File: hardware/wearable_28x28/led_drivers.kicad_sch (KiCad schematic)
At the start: 22 parts, among them U101 MBI5124GP-B, U102 MBI5124GP-B, U103 MBI5124GP-B, U104 MBI5124GP-B, U105 MBI5124GP-B, U106 MBI5124GP-B, U107 SN74LVC1G125DBVR

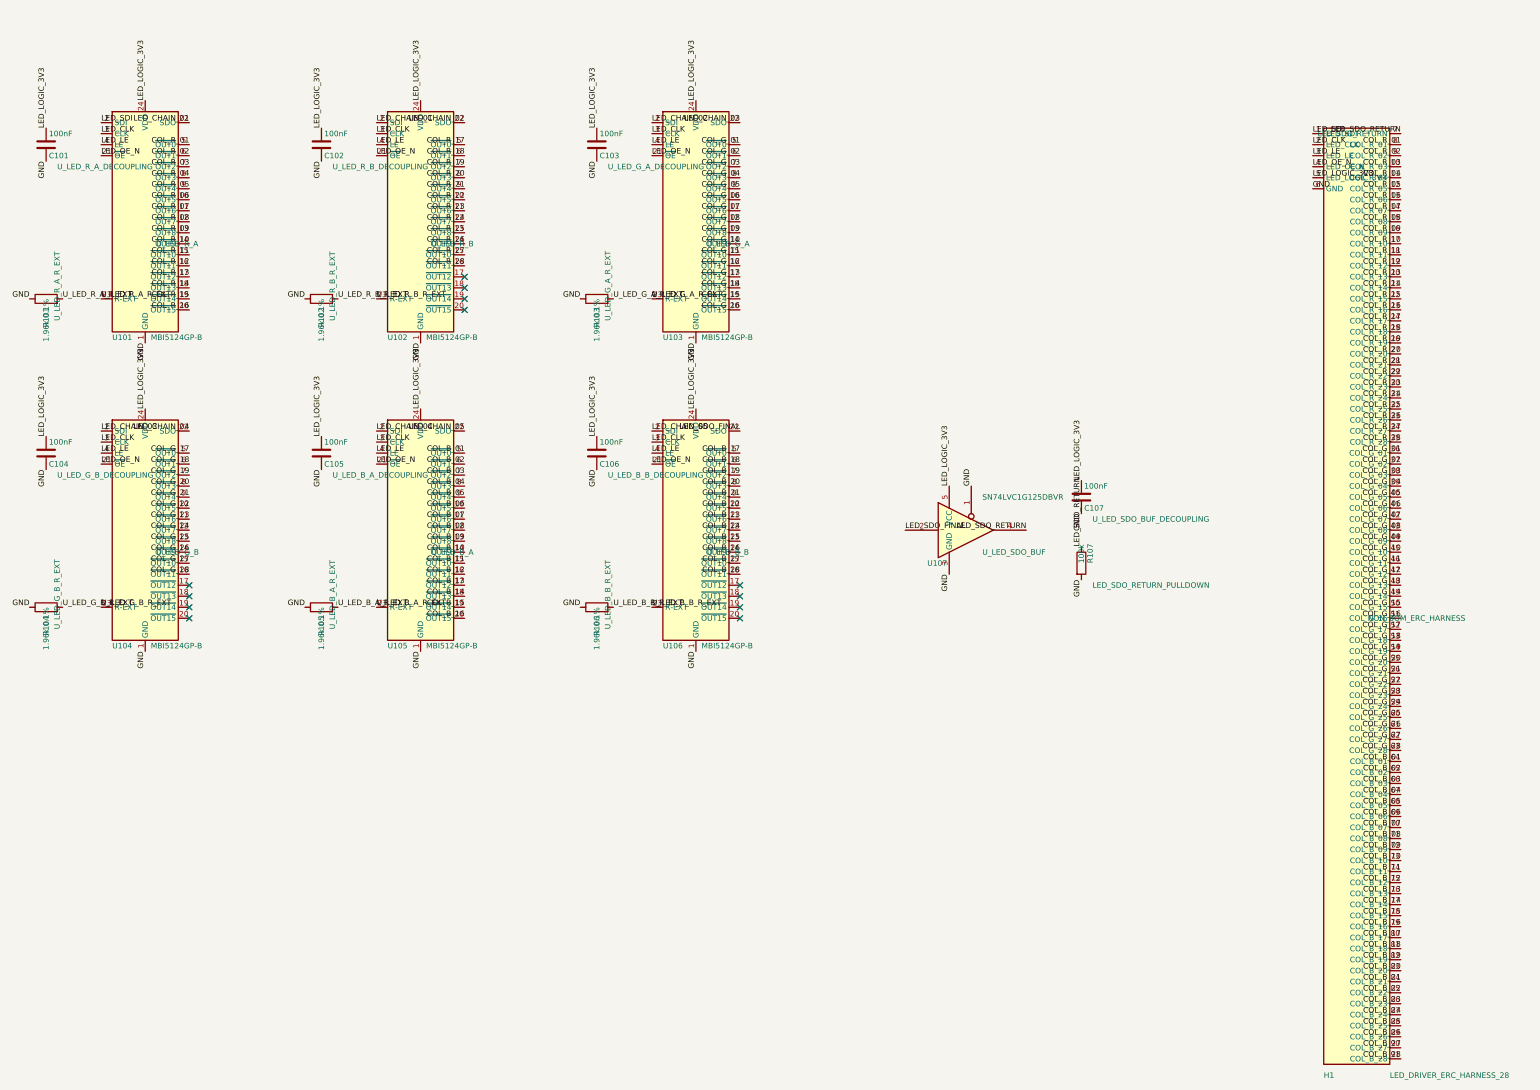
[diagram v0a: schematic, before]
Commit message: Generate complete conditional schematic hierarchy
Co-authored-by: illiapliukhin <illiapliukhin@users.noreply.github.com>
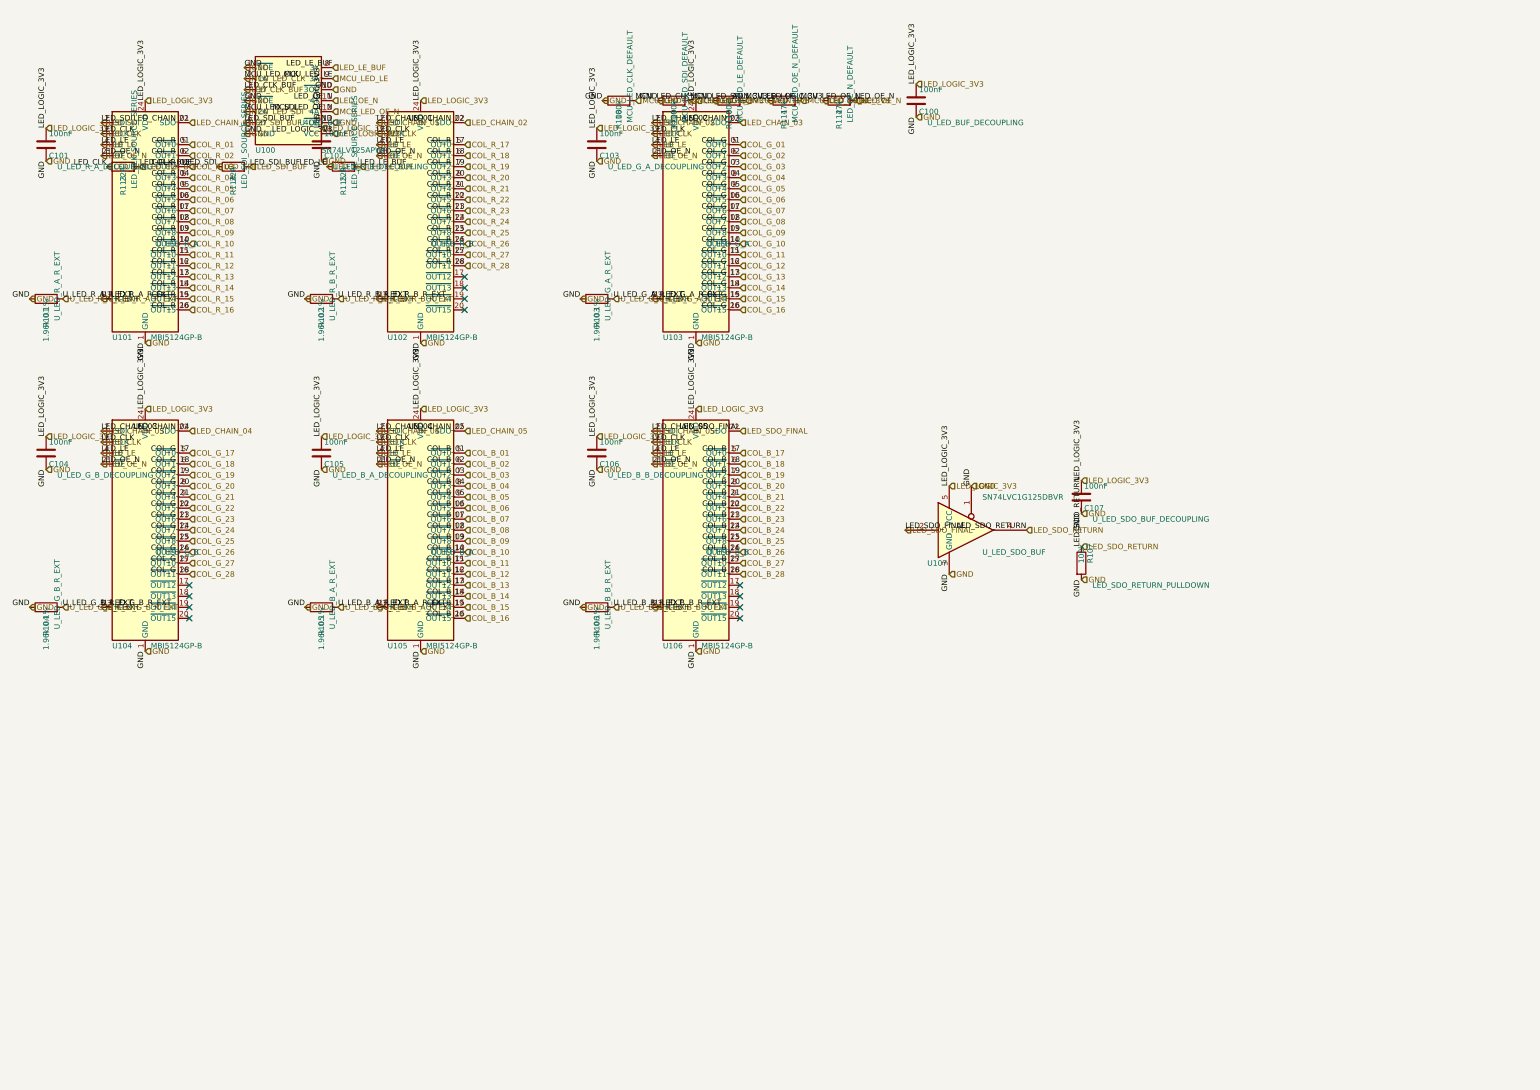
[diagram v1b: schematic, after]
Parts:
- removed H1: LED_DRIVER_ERC_HARNESS_28, symbol PartSignal_Wearable:LED_DRIVER_ERC_HARNESS_28
- added C100: 100nF, Capacitor_SMD:C_0603_1608Metric, symbol Device:C
- added R108, R109, R110: 100k, Resistor_SMD:R_0603_1608Metric, symbol Device:R
- added R111, R112: 47k, Resistor_SMD:R_0603_1608Metric, symbol Device:R
- added R113, R114, R115: 22R, Resistor_SMD:R_0603_1608Metric, symbol Device:R
- added U100: SN74LV125APWR, Package_SO:TSSOP-14_4.4x5mm_P0.65mm, symbol PartSignal_Wearable:SN74LV125APWR
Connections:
- net GND: now also C100.2, R108.1, R109.1, R110.1, U100.1 (~{1OE}), U100.10 (~{3OE}), U100.13 (~{4OE}), U100.4 (~{2OE}), U100.7 (GND)
- net LED_CLK: now also R113.1
- net LED_LE: now also R115.1
- net LED_LOGIC_3V3: now also C100.1, R112.1, U100.14 (VCC)
- net LED_OE_N: now also R112.2, U100.11 (4Y)
- net LED_SDI: now also R114.1
- new net AON_3V3: R111.1
- new net LED_CLK_BUF: R113.2, U100.3 (1Y)
- new net LED_LE_BUF: R115.2, U100.8 (3Y)
- new net LED_SDI_BUF: R114.2, U100.6 (2Y)
- new net MCU_LED_CLK: R108.2, U100.2 (1A)
- new net MCU_LED_LE: R110.2, U100.9 (3A)
- new net MCU_LED_OE_N: R111.2, U100.12 (4A)
- new net MCU_LED_SDI: R109.2, U100.5 (2A)
